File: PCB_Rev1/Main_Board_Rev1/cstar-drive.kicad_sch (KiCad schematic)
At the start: 2 parts, among them J12 532610771, J9 532610771

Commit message: Revert "Audio subsystem re-created"
This reverts commit 6dc47edf88eae56b01440ce5f2dfd5da155ce597.
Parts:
- removed J12, J9: 532610771, Connector_Molex:Molex_PicoBlade_53261-0771_1x07-1MP_P1.25mm_Horizontal, symbol 532610771:532610771
- added C15: 100nF, Capacitor_SMD:C_0805_2012Metric, symbol Device:C
- added C16: 220uF, Footprints:Cap_Polarized_220uF, symbol Device:C_Polarized
- added D2, D3, D4, D5, D6, D7, D8, D9: D, Footprints:Diode_1N4007, symbol Device:D
- added J10, J9: B4B-PH-K-S, Footprints:B4B_PH_K_S, symbol B4B_PH_K_S:B4B-PH-K-S
- added U2: L298N, Package_TO_SOT_THT:TO-220-15_P2.54x2.54mm_StaggerOdd_Lead4.58mm_Vertical, symbol Driver_Motor:L298N
- added X1, X2: B2P-VH, Footprints:B2P-VH, symbol B2P-VH:B2P-VH
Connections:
- net +5V: now also C15.1, U2.9 (Vss)
- net GND: now also C15.2, C16.2, D3.2 (A), D5.2 (A), D7.2 (A), D9.2 (A), J10.2, J9.2, U2.1 (SENSE_A), U2.15 (SENSE_B), U2.8 (GND)
- new net +12V: C16.1, D2.1 (K), D4.1 (K), D6.1 (K), D8.1 (K), U2.4 (Vs)
- new net +3V3: J10.1, J9.1
- new net Ch.A_MOTOR_1: J9.3
- new net Ch.A_MOTOR_2: J10.3
- new net Ch.B_MOTOR_1: J9.4
- new net Ch.B_MOTOR_2: J10.4
- new net EN_MOTOR_1: U2.6 (EnA)
- new net EN_MOTOR_2: U2.11 (EnB)
- new net IN1_MOTOR_1: U2.5 (IN1)
- new net IN1_MOTOR_2: U2.10 (IN3)
- new net IN2_MOTOR_1: U2.7 (IN2)
- new net IN2_MOTOR_2: U2.12 (IN4)
- new net OUT1_MOTOR_1: D2.2 (A), D3.1 (K), U2.2 (OUT1), X1.1
- new net OUT1_MOTOR_2: D6.2 (A), D7.1 (K), U2.13 (OUT3), X2.1
- new net OUT2_MOTOR_1: D4.2 (A), D5.1 (K), U2.3 (OUT2), X1.2
- new net OUT2_MOTOR_2: D8.2 (A), D9.1 (K), U2.14 (OUT4), X2.2
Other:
- note added: "ENCODER 1 CONNECTION"
- note added: "ENCODER 2 CONNECTION"
- note added: "MOTOR 1 CONNECTION"
- note added: "MOTOR 2 CONNECTION"
- note added: "MOTOR DRIVE TRAIN SCHEMATIC"
- note added: "MOTOR DRIVER"
- note removed: "Lidar Connector"

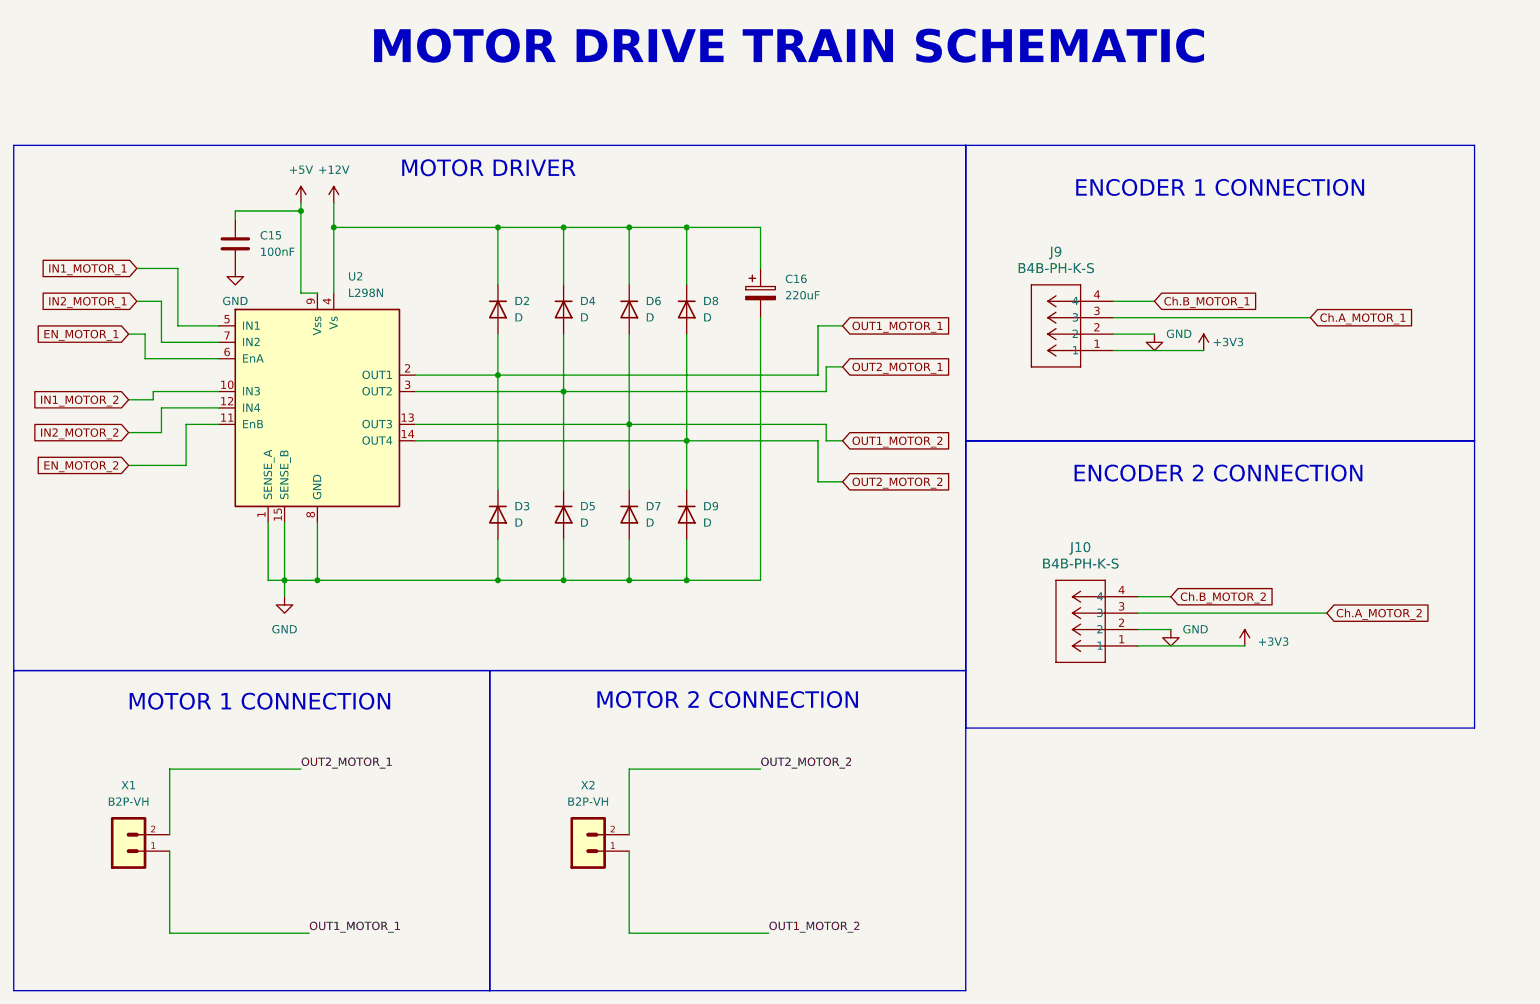
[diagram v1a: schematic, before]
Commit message: Audio subsystem re-created
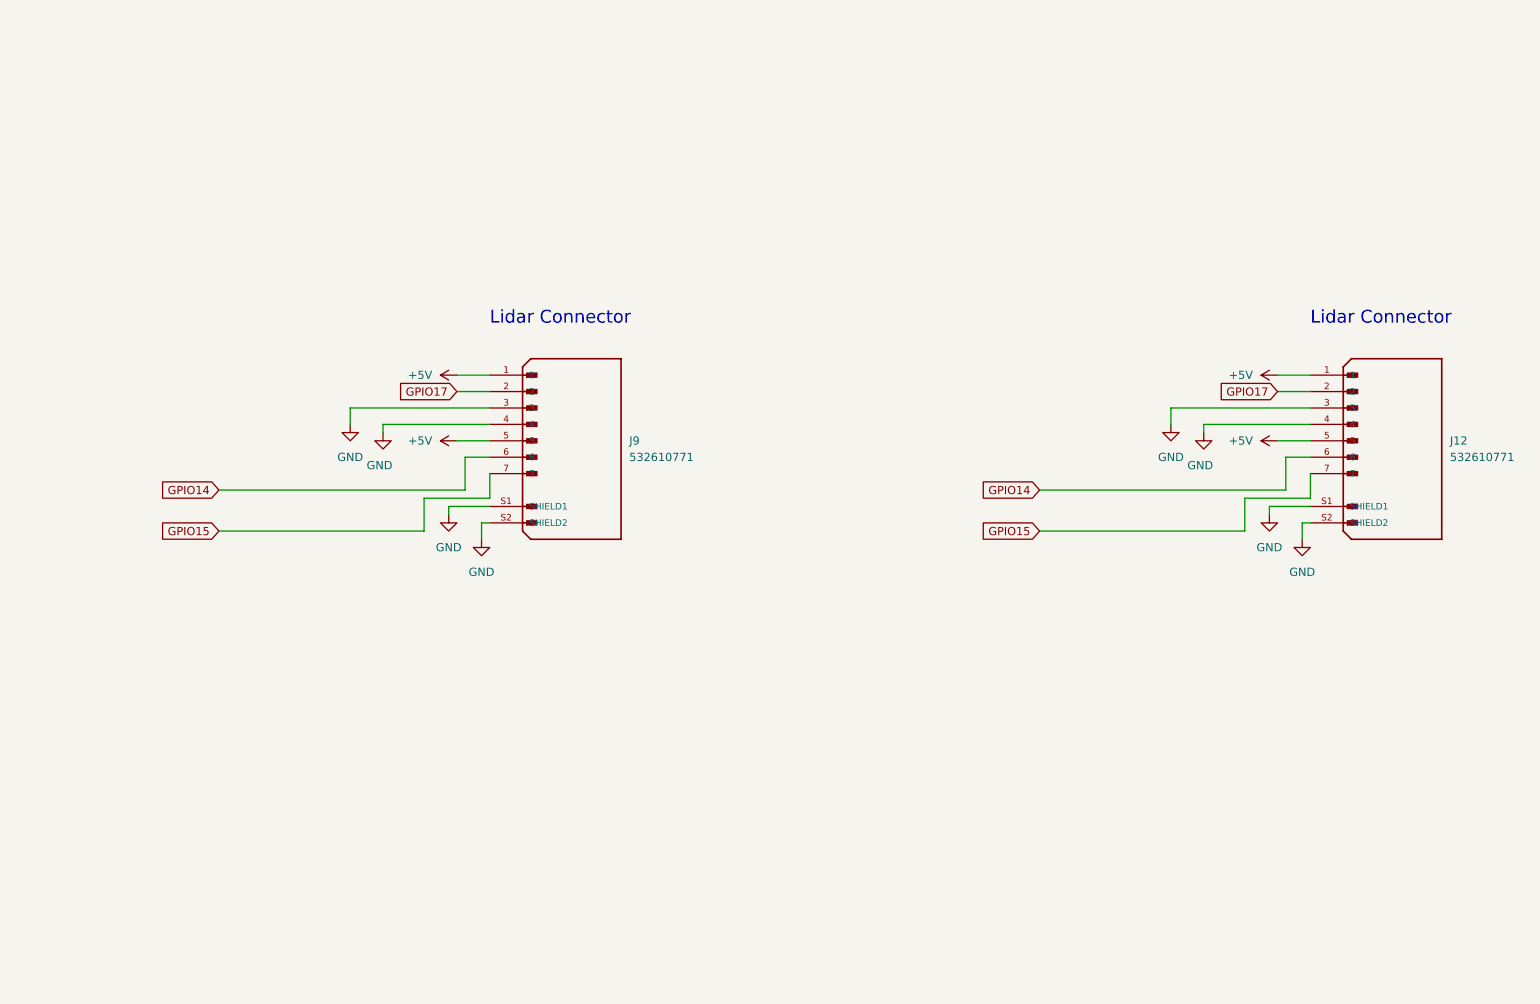
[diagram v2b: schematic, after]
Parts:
- removed C15: 100nF, Capacitor_SMD:C_0805_2012Metric, symbol Device:C
- removed C16: 220uF, Footprints:Cap_Polarized_220uF, symbol Device:C_Polarized
- removed D2, D3, D4, D5, D6, D7, D8, D9: D, Footprints:Diode_1N4007, symbol Device:D
- removed J10, J9: B4B-PH-K-S, Footprints:B4B_PH_K_S, symbol B4B_PH_K_S:B4B-PH-K-S
- removed U2: L298N, Package_TO_SOT_THT:TO-220-15_P2.54x2.54mm_StaggerOdd_Lead4.58mm_Vertical, symbol Driver_Motor:L298N
- removed X1, X2: B2P-VH, Footprints:B2P-VH, symbol B2P-VH:B2P-VH
- added J12, J9: 532610771, Connector_Molex:Molex_PicoBlade_53261-0771_1x07-1MP_P1.25mm_Horizontal, symbol 532610771:532610771
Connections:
- net +5V: now also J12.1, J12.5, J9.1, J9.5
- net GND: now also J12.3, J12.4, J12.S1 (SHIELD1), J12.S2 (SHIELD2), J9.3, J9.4, J9.S1 (SHIELD1), J9.S2 (SHIELD2)
- new net GPIO14: J12.6, J9.6
- new net GPIO15: J12.7, J9.7
- new net GPIO17: J12.2, J9.2
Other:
- note added: "Lidar Connector"
- note removed: "ENCODER 1 CONNECTION"
- note removed: "ENCODER 2 CONNECTION"
- note removed: "MOTOR 1 CONNECTION"
- note removed: "MOTOR 2 CONNECTION"
- note removed: "MOTOR DRIVE TRAIN SCHEMATIC"
- note removed: "MOTOR DRIVER"

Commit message: Audio Back
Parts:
- renumbered J9 to J10, J12 to J13
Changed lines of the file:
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@@
 		(dnp no)
 		(fields_autoplaced yes)
-		(property "Reference" "#PWR038"
+		(property "Reference" "#PWR049"
 			(at 97.79 88.9 0)
 			(effects
@@
 					(unit 1)
 				)
-				(path "/8f5a23de-a1fa-4202-92fb-c2ac3de0338c/b82e2994-3828-4951-9572-d8060e0d0a41"
-					(reference "#PWR038")
-					(unit 1)
-				)
 			)
 		)
@@
 		(dnp no)
 		(fields_autoplaced yes)
-		(property "Reference" "J9"
+		(property "Reference" "J10"
 			(at 120.65 88.9 0)
 			(effects
@@
 					(unit 1)
 				)
-				(path "/8f5a23de-a1fa-4202-92fb-c2ac3de0338c/b82e2994-3828-4951-9572-d8060e0d0a41"
-					(reference "J9")
-					(unit 1)
-				)
 			)
 		)
@@
 		(dnp no)
 		(fields_autoplaced yes)
-		(property "Reference" "#PWR056"
+		(property "Reference" "#PWR062"
 			(at 224.79 110.49 0)
 			(effects
@@
 					(unit 1)
 				)
-				(path "/8f5a23de-a1fa-4202-92fb-c2ac3de0338c/b82e2994-3828-4951-9572-d8060e0d0a41"
-					(reference "#PWR056")
-					(unit 1)
-				)
 			)
 		)
@@
 		(dnp no)
 		(fields_autoplaced yes)
-		(property "Reference" "#PWR036"
+		(property "Reference" "#PWR047"
 			(at 92.71 106.68 0)
 			(effects
@@
 					(unit 1)
 				)
-				(path "/8f5a23de-a1fa-4202-92fb-c2ac3de0338c/b82e2994-3828-4951-9572-d8060e0d0a41"
-					(reference "#PWR036")
-					(unit 1)
-				)
 			)
 		)
@@
 		(dnp no)
 		(fields_autoplaced yes)
-		(property "Reference" "#PWR055"
+		(property "Reference" "#PWR061"
 			(at 224.79 88.9 0)
 			(effects
@@
 					(unit 1)
 				)
-				(path "/8f5a23de-a1fa-4202-92fb-c2ac3de0338c/b82e2994-3828-4951-9572-d8060e0d0a41"
-					(reference "#PWR055")
-					(unit 1)
-				)
 			)
 		)
@@
 		(dnp no)
 		(fields_autoplaced yes)
-		(property "Reference" "#PWR037"
+		(property "Reference" "#PWR048"
 			(at 97.79 78.74 0)
 			(effects
@@
 					(unit 1)
 				)
-				(path "/8f5a23de-a1fa-4202-92fb-c2ac3de0338c/b82e2994-3828-4951-9572-d8060e0d0a41"
-					(reference "#PWR037")
-					(unit 1)
-				)
 			)
 		)
@@
 		(dnp no)
 		(fields_autoplaced yes)
-		(property "Reference" "#PWR054"
+		(property "Reference" "#PWR060"
 			(at 224.79 78.74 0)
 			(effects
@@
 					(unit 1)
 				)
-				(path "/8f5a23de-a1fa-4202-92fb-c2ac3de0338c/b82e2994-3828-4951-9572-d8060e0d0a41"
-					(reference "#PWR054")
-					(unit 1)
-				)
 			)
 		)
@@
 		(dnp no)
 		(fields_autoplaced yes)
-		(property "Reference" "#PWR051"
+		(property "Reference" "#PWR057"
 			(at 204.47 92.71 0)
 			(effects
@@
 					(unit 1)
 				)
-				(path "/8f5a23de-a1fa-4202-92fb-c2ac3de0338c/b82e2994-3828-4951-9572-d8060e0d0a41"
-					(reference "#PWR051")
-					(unit 1)
-				)
 			)
 		)
@@
 		(on_board yes)
 		(dnp no)
-		(property "Reference" "#PWR035"
+		(property "Reference" "#PWR046"
 			(at 82.55 93.98 0)
 			(effects
@@
 					(unit 1)
 				)
-				(path "/8f5a23de-a1fa-4202-92fb-c2ac3de0338c/b82e2994-3828-4951-9572-d8060e0d0a41"
-					(reference "#PWR035")
-					(unit 1)
-				)
 			)
 		)
@@
 		(dnp no)
 		(fields_autoplaced yes)
-		(property "Reference" "#PWR053"
+		(property "Reference" "#PWR059"
 			(at 219.71 106.68 0)
 			(effects
@@
 					(unit 1)
 				)
-				(path "/8f5a23de-a1fa-4202-92fb-c2ac3de0338c/b82e2994-3828-4951-9572-d8060e0d0a41"
-					(reference "#PWR053")
-					(unit 1)
-				)
 			)
 		)
@@
 		(on_board yes)
 		(dnp no)
-		(property "Reference" "#PWR052"
+		(property "Reference" "#PWR058"
 			(at 209.55 93.98 0)
 			(effects
@@
 					(unit 1)
 				)
-				(path "/8f5a23de-a1fa-4202-92fb-c2ac3de0338c/b82e2994-3828-4951-9572-d8060e0d0a41"
-					(reference "#PWR052")
-					(unit 1)
-				)
 			)
 		)
@@
 		(dnp no)
 		(fields_autoplaced yes)
-		(property "Reference" "J12"
+		(property "Reference" "J13"
 			(at 247.65 88.9 0)
 			(effects
@@
 					(unit 1)
 				)
-				(path "/8f5a23de-a1fa-4202-92fb-c2ac3de0338c/b82e2994-3828-4951-9572-d8060e0d0a41"
-					(reference "J12")
-					(unit 1)
-				)
 			)
 		)
@@
 		(dnp no)
 		(fields_autoplaced yes)
-		(property "Reference" "#PWR034"
+		(property "Reference" "#PWR045"
 			(at 77.47 92.71 0)
 			(effects
@@
 					(unit 1)
 				)
-				(path "/8f5a23de-a1fa-4202-92fb-c2ac3de0338c/b82e2994-3828-4951-9572-d8060e0d0a41"
-					(reference "#PWR034")
-					(unit 1)
-				)
 			)
 		)
@@
 		(dnp no)
 		(fields_autoplaced yes)
-		(property "Reference" "#PWR039"
+		(property "Reference" "#PWR050"
 			(at 97.79 110.49 0)
 			(effects
@@
 					(unit 1)
 				)
-				(path "/8f5a23de-a1fa-4202-92fb-c2ac3de0338c/b82e2994-3828-4951-9572-d8060e0d0a41"
-					(reference "#PWR039")
-					(unit 1)
-				)

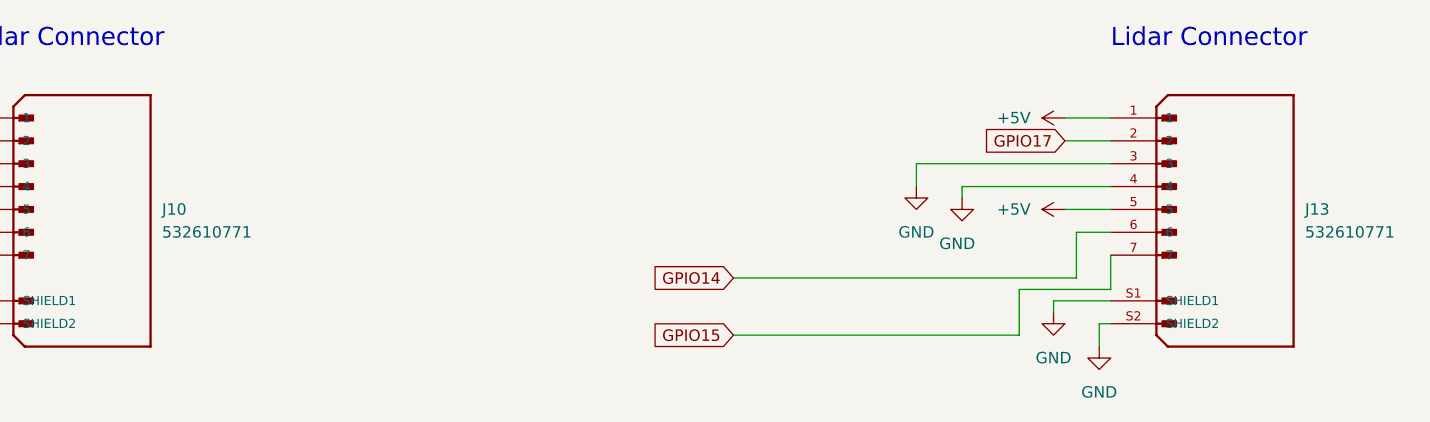
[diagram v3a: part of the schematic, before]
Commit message: Revert "Audio Back"
This reverts commit b4c952123ee183b7f2e3a0aacd1af0ad900a0b00.
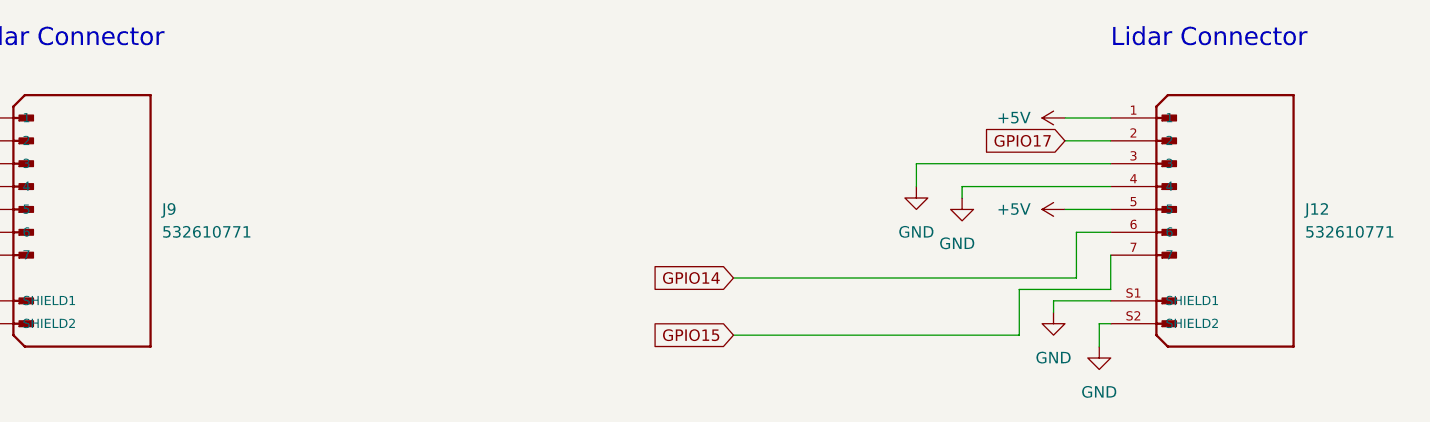
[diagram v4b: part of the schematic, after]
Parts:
- renumbered J13 to J12, J10 to J9
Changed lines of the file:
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@@
 		(dnp no)
 		(fields_autoplaced yes)
-		(property "Reference" "#PWR049"
+		(property "Reference" "#PWR038"
 			(at 97.79 88.9 0)
 			(effects
@@
 				(path "/8f5a23de-a1fa-4202-92fb-c2ac3de0338c/0ea4e72d-54a3-4446-a173-a8fc45c421fe"
 					(reference "#PWR049")
+					(unit 1)
+				)
+				(path "/8f5a23de-a1fa-4202-92fb-c2ac3de0338c/b82e2994-3828-4951-9572-d8060e0d0a41"
+					(reference "#PWR038")
 					(unit 1)
 				)
@@
 		(dnp no)
 		(fields_autoplaced yes)
-		(property "Reference" "J10"
+		(property "Reference" "J9"
 			(at 120.65 88.9 0)
 			(effects
@@
 				(path "/8f5a23de-a1fa-4202-92fb-c2ac3de0338c/0ea4e72d-54a3-4446-a173-a8fc45c421fe"
 					(reference "J10")
+					(unit 1)
+				)
+				(path "/8f5a23de-a1fa-4202-92fb-c2ac3de0338c/b82e2994-3828-4951-9572-d8060e0d0a41"
+					(reference "J9")
 					(unit 1)
 				)
@@
 		(dnp no)
 		(fields_autoplaced yes)
-		(property "Reference" "#PWR062"
+		(property "Reference" "#PWR056"
 			(at 224.79 110.49 0)
 			(effects
@@
 				(path "/8f5a23de-a1fa-4202-92fb-c2ac3de0338c/0ea4e72d-54a3-4446-a173-a8fc45c421fe"
 					(reference "#PWR062")
+					(unit 1)
+				)
+				(path "/8f5a23de-a1fa-4202-92fb-c2ac3de0338c/b82e2994-3828-4951-9572-d8060e0d0a41"
+					(reference "#PWR056")
 					(unit 1)
 				)
@@
 		(dnp no)
 		(fields_autoplaced yes)
-		(property "Reference" "#PWR047"
+		(property "Reference" "#PWR036"
 			(at 92.71 106.68 0)
 			(effects
@@
 				(path "/8f5a23de-a1fa-4202-92fb-c2ac3de0338c/0ea4e72d-54a3-4446-a173-a8fc45c421fe"
 					(reference "#PWR047")
+					(unit 1)
+				)
+				(path "/8f5a23de-a1fa-4202-92fb-c2ac3de0338c/b82e2994-3828-4951-9572-d8060e0d0a41"
+					(reference "#PWR036")
 					(unit 1)
 				)
@@
 		(dnp no)
 		(fields_autoplaced yes)
-		(property "Reference" "#PWR061"
+		(property "Reference" "#PWR055"
 			(at 224.79 88.9 0)
 			(effects
@@
 				(path "/8f5a23de-a1fa-4202-92fb-c2ac3de0338c/0ea4e72d-54a3-4446-a173-a8fc45c421fe"
 					(reference "#PWR061")
+					(unit 1)
+				)
+				(path "/8f5a23de-a1fa-4202-92fb-c2ac3de0338c/b82e2994-3828-4951-9572-d8060e0d0a41"
+					(reference "#PWR055")
 					(unit 1)
 				)
@@
 		(dnp no)
 		(fields_autoplaced yes)
-		(property "Reference" "#PWR048"
+		(property "Reference" "#PWR037"
 			(at 97.79 78.74 0)
 			(effects
@@
 				(path "/8f5a23de-a1fa-4202-92fb-c2ac3de0338c/0ea4e72d-54a3-4446-a173-a8fc45c421fe"
 					(reference "#PWR048")
+					(unit 1)
+				)
+				(path "/8f5a23de-a1fa-4202-92fb-c2ac3de0338c/b82e2994-3828-4951-9572-d8060e0d0a41"
+					(reference "#PWR037")
 					(unit 1)
 				)
@@
 		(dnp no)
 		(fields_autoplaced yes)
-		(property "Reference" "#PWR060"
+		(property "Reference" "#PWR054"
 			(at 224.79 78.74 0)
 			(effects
@@
 				(path "/8f5a23de-a1fa-4202-92fb-c2ac3de0338c/0ea4e72d-54a3-4446-a173-a8fc45c421fe"
 					(reference "#PWR060")
+					(unit 1)
+				)
+				(path "/8f5a23de-a1fa-4202-92fb-c2ac3de0338c/b82e2994-3828-4951-9572-d8060e0d0a41"
+					(reference "#PWR054")
 					(unit 1)
 				)
@@
 		(dnp no)
 		(fields_autoplaced yes)
-		(property "Reference" "#PWR057"
+		(property "Reference" "#PWR051"
 			(at 204.47 92.71 0)
 			(effects
@@
 				(path "/8f5a23de-a1fa-4202-92fb-c2ac3de0338c/0ea4e72d-54a3-4446-a173-a8fc45c421fe"
 					(reference "#PWR057")
+					(unit 1)
+				)
+				(path "/8f5a23de-a1fa-4202-92fb-c2ac3de0338c/b82e2994-3828-4951-9572-d8060e0d0a41"
+					(reference "#PWR051")
 					(unit 1)
 				)
@@
 		(on_board yes)
 		(dnp no)
-		(property "Reference" "#PWR046"
+		(property "Reference" "#PWR035"
 			(at 82.55 93.98 0)
 			(effects
@@
 				(path "/8f5a23de-a1fa-4202-92fb-c2ac3de0338c/0ea4e72d-54a3-4446-a173-a8fc45c421fe"
 					(reference "#PWR046")
+					(unit 1)
+				)
+				(path "/8f5a23de-a1fa-4202-92fb-c2ac3de0338c/b82e2994-3828-4951-9572-d8060e0d0a41"
+					(reference "#PWR035")
 					(unit 1)
 				)
@@
 		(dnp no)
 		(fields_autoplaced yes)
-		(property "Reference" "#PWR059"
+		(property "Reference" "#PWR053"
 			(at 219.71 106.68 0)
 			(effects
@@
 				(path "/8f5a23de-a1fa-4202-92fb-c2ac3de0338c/0ea4e72d-54a3-4446-a173-a8fc45c421fe"
 					(reference "#PWR059")
+					(unit 1)
+				)
+				(path "/8f5a23de-a1fa-4202-92fb-c2ac3de0338c/b82e2994-3828-4951-9572-d8060e0d0a41"
+					(reference "#PWR053")
 					(unit 1)
 				)
@@
 		(on_board yes)
 		(dnp no)
-		(property "Reference" "#PWR058"
+		(property "Reference" "#PWR052"
 			(at 209.55 93.98 0)
 			(effects
@@
 				(path "/8f5a23de-a1fa-4202-92fb-c2ac3de0338c/0ea4e72d-54a3-4446-a173-a8fc45c421fe"
 					(reference "#PWR058")
+					(unit 1)
+				)
+				(path "/8f5a23de-a1fa-4202-92fb-c2ac3de0338c/b82e2994-3828-4951-9572-d8060e0d0a41"
+					(reference "#PWR052")
 					(unit 1)
 				)
@@
 		(dnp no)
 		(fields_autoplaced yes)
-		(property "Reference" "J13"
+		(property "Reference" "J12"
 			(at 247.65 88.9 0)
 			(effects
@@
 				(path "/8f5a23de-a1fa-4202-92fb-c2ac3de0338c/0ea4e72d-54a3-4446-a173-a8fc45c421fe"
 					(reference "J13")
+					(unit 1)
+				)
+				(path "/8f5a23de-a1fa-4202-92fb-c2ac3de0338c/b82e2994-3828-4951-9572-d8060e0d0a41"
+					(reference "J12")
 					(unit 1)
 				)
@@
 		(dnp no)
 		(fields_autoplaced yes)
-		(property "Reference" "#PWR045"
+		(property "Reference" "#PWR034"
 			(at 77.47 92.71 0)
 			(effects
@@
 				(path "/8f5a23de-a1fa-4202-92fb-c2ac3de0338c/0ea4e72d-54a3-4446-a173-a8fc45c421fe"
 					(reference "#PWR045")
+					(unit 1)
+				)
+				(path "/8f5a23de-a1fa-4202-92fb-c2ac3de0338c/b82e2994-3828-4951-9572-d8060e0d0a41"
+					(reference "#PWR034")
 					(unit 1)
 				)
@@
 		(dnp no)
 		(fields_autoplaced yes)
-		(property "Reference" "#PWR050"
+		(property "Reference" "#PWR039"
 			(at 97.79 110.49 0)
 			(effects
@@
 					(unit 1)
 				)
+				(path "/8f5a23de-a1fa-4202-92fb-c2ac3de0338c/b82e2994-3828-4951-9572-d8060e0d0a41"
+					(reference "#PWR039")
+					(unit 1)
+				)
